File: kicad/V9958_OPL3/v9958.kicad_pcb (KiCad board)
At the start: 2 copper layers, 160 x 100.3 mm, 54 parts, among them P1 RED, P2 GREEN, P3 BLUE, P4 SYNC/C, P5 CONN_02X25, U1 74HCT139, U2 V9958, U3 DRAM_64KX4, U4 DRAM_64KX4, U5 DRAM_64KX4, U6 DRAM_64KX4, U7 cxa2075M, X1 OSC, X2 S-VIDEO, Y1 21,443Mhz

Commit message: update
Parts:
- removed C12, C9: 100n, Capacitors_ThroughHole:C_Disc_D3_P2.5
- removed X2: S-VIDEO, mini_din:mini_din-M_DIN4
- added C22: 220µF, Capacitors_ThroughHole:C_Radial_D6.3_L11.2_P2.5, F.Cu at (83.8, 88.9)
- added C23: 220µF, Capacitors_ThroughHole:C_Radial_D6.3_L11.2_P2.5, F.Cu at (83.8, 101.6)
- added U8: YMF262, Housings_SOIC:SOIC-24_7.5x15.4mm_Pitch1.27mm, F.Cu at (195.6, 71.1)
- added U9: YAC512, Housings_SOIC:SOIC-16_3.9x9.9mm_Pitch1.27mm, F.Cu at (150.2, 133.0)
- added X3: S-VIDEO, mini_din:mini_din-M_DIN4, F.Cu at (66.0, 124.5)
- C11: value 47µF -> 100n; footprint Capacitors_ThroughHole:C_Radial_D5_L11_P2.5 -> Capacitors_ThroughHole:C_Disc_D3_P2.5
- C13, C19: value 100n -> 47µF
- C14, C15, C21: value 220µF -> 100n; footprint Capacitors_ThroughHole:C_Radial_D6.3_L11.2_P2.5 -> Capacitors_ThroughHole:C_Disc_D3_P2.5
- C17: value 47µF -> 220µF; footprint Capacitors_ThroughHole:C_Radial_D5_L11_P2.5 -> Capacitors_ThroughHole:C_Radial_D6.3_L11.2_P2.5
- moved C15 110.8 mm to (194.3, 54.6), turned to 0 degrees
- moved C14 87.7 mm to (171.4, 116.8)
- moved C21 65.9 mm to (143.5, 129.5), turned to 270 degrees
- moved C11 53.8 mm to (171.4, 119.4), turned to 180 degrees
- moved C18 52.1 mm to (83.8, 128.3)
- moved C17 27.9 mm to (83.8, 63.5)
- moved C10 16.5 mm to (177.8, 129.5)
- moved C20 12.7 mm to (83.8, 76.2)
- moved C16 7.62 mm to (83.8, 120.7)
- moved R11 2.54 mm to (91.4, 99.1)
- moved R12 2.54 mm to (91.4, 96.5)
- moved C19 2.54 mm to (106.7, 82.5)
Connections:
- net /CSYNC renamed /cxa2075m/CSYNC
- C10 pad 1: /RGB_G -> VCC
- C10 pad 2: Net-(C10-Pad2) -> GND
- C11 pad 1: VCC -> /cxa2075m/RGB_B
- C11 pad 2: GND -> Net-(C11-Pad2)
- C14 pad 1: Net-(C14-Pad1) -> /cxa2075m/RGB_R
- C14 pad 2: /C_OUT -> Net-(C14-Pad2)
- C15 pad 1: Net-(C15-Pad1) -> VCC
- C15 pad 2: Net-(C15-Pad2) -> GND
- C16 pad 2: /Y_OUT -> /cxa2075m/C_OUT
- C17 pad 1: VCC -> Net-(C17-Pad1)
- C17 pad 2: GND -> Net-(C17-Pad2)
- C18 pad 2: Net-(C18-Pad2) -> /cxa2075m/Y_OUT
- C21 pad 1: Net-(C21-Pad1) -> VCC
- C21 pad 2: Net-(C21-Pad2) -> GND
- P1 pad 1: Net-(C15-Pad2) -> Net-(C17-Pad2)
- P2 pad 1: Net-(C18-Pad2) -> Net-(C20-Pad2)
- P3 pad 1: Net-(C20-Pad2) -> Net-(C22-Pad2)
- P4 pad 1: Net-(C21-Pad2) -> Net-(C23-Pad2)
- R1 pad 2: /RGB_G -> /cxa2075m/RGB_G
- R11 pad 2: Net-(C16-Pad1) -> Net-(C18-Pad1)
- R12 pad 2: Net-(C14-Pad1) -> Net-(C16-Pad1)
- R13 pad 1: Net-(C21-Pad1) -> Net-(C23-Pad1)
- R2 pad 2: /RGB_R -> /cxa2075m/RGB_R
- R3 pad 2: /RGB_B -> /cxa2075m/RGB_B
- R6 pad 2: Net-(C15-Pad1) -> Net-(C17-Pad1)
- R7 pad 2: Net-(C18-Pad1) -> Net-(C20-Pad1)
- R8 pad 2: Net-(C20-Pad1) -> Net-(C22-Pad1)
- R9 pad 2: Net-(C21-Pad1) -> Net-(C23-Pad1)
- U1 pad 10: (no net) -> Net-(U1-Pad10)
- U1 pad 11: (no net) -> Net-(U1-Pad11)
- U1 pad 12: (no net) -> Net-(U1-Pad12)
- U1 pad 13: (no net) -> GND
- U1 pad 14: (no net) -> /RW
- U1 pad 15: (no net) -> /CS_IO0
- U1 pad 9: (no net) -> Net-(U1-Pad9)
- U2 pad 22: /RGB_G -> /cxa2075m/RGB_G
- U2 pad 23: /RGB_R -> /cxa2075m/RGB_R
- U2 pad 24: /RGB_B -> /cxa2075m/RGB_B
- U7 pad 2: Net-(C12-Pad2) -> Net-(C14-Pad2)
- U7 pad 3: Net-(C10-Pad2) -> Net-(C12-Pad2)
- U7 pad 4: Net-(C9-Pad2) -> Net-(C11-Pad2)
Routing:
- net Net-(C11-Pad2): track 0.00 -> 146.6 mm
- net Net-(C9-Pad2): track 75.5 -> 0.00 mm
- net VCC: track 364.5 -> 292.0 mm
- net Net-(C10-Pad2): track 71.5 -> 0.00 mm
- net GND: track 576.9 -> 617.3 mm
- net Net-(C14-Pad1): track 26.1 -> 0.00 mm
- net Net-(C17-Pad1): track 0.00 -> 23.2 mm
- net Net-(C15-Pad1): track 23.2 -> 0.00 mm
- net Net-(C23-Pad1): track 0.00 -> 20.4 mm
- net Net-(C21-Pad1): track 20.4 -> 0.00 mm
- net Net-(C16-Pad1): track 39.0 -> 58.2 mm
- net /cxa2075m/RGB_B: track 0.00 -> 13.1 mm
- net /RGB_B: track 13.1 -> 0.00 mm
- net Net-(R12-Pad1): track 26.8 -> 39.4 mm
- net Net-(R11-Pad1): track 24.1 -> 11.5 mm
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
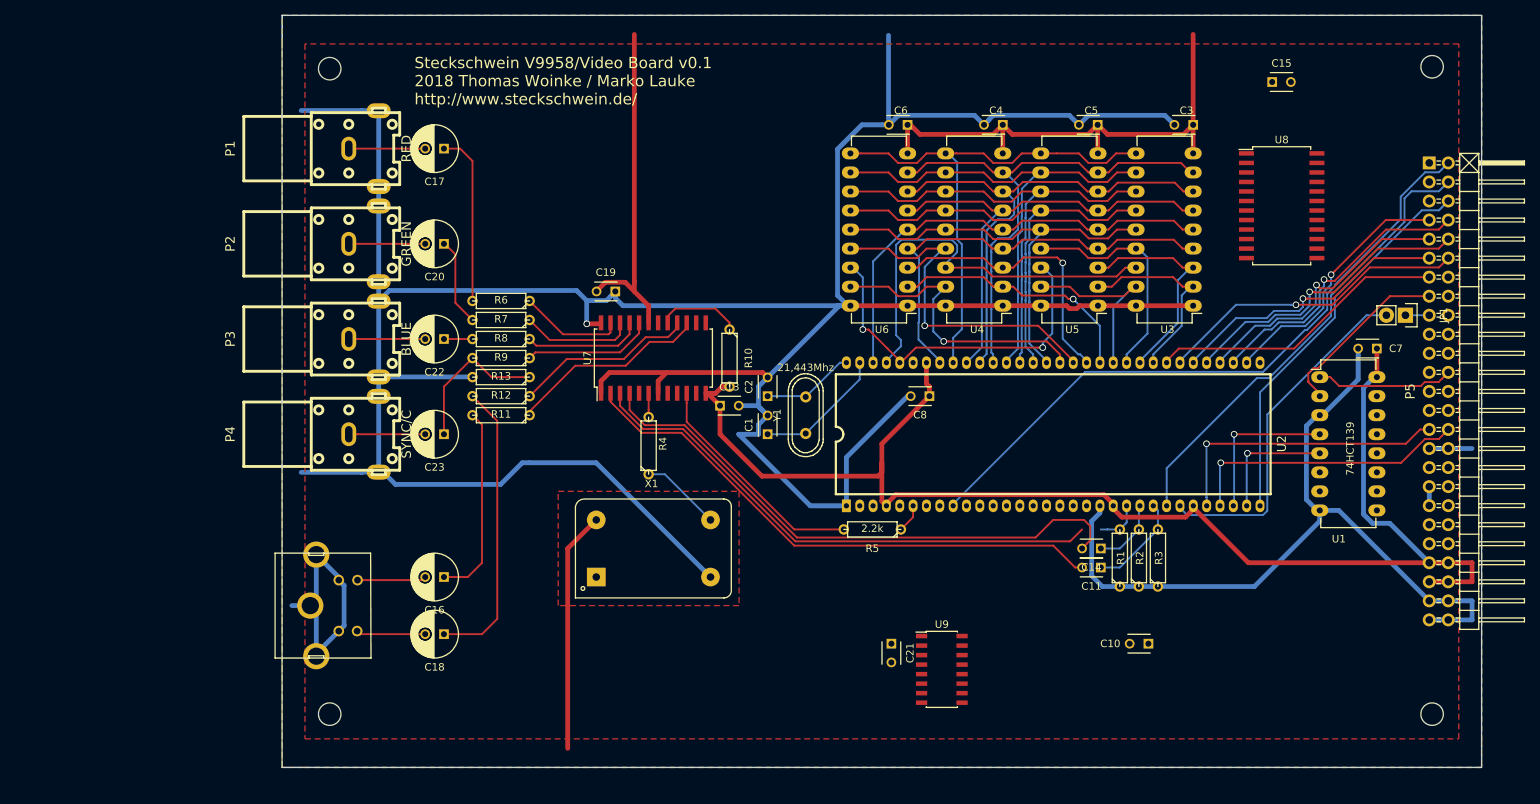
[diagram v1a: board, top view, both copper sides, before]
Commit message: dsub9-connector for RGB, pinout like 1084S D2
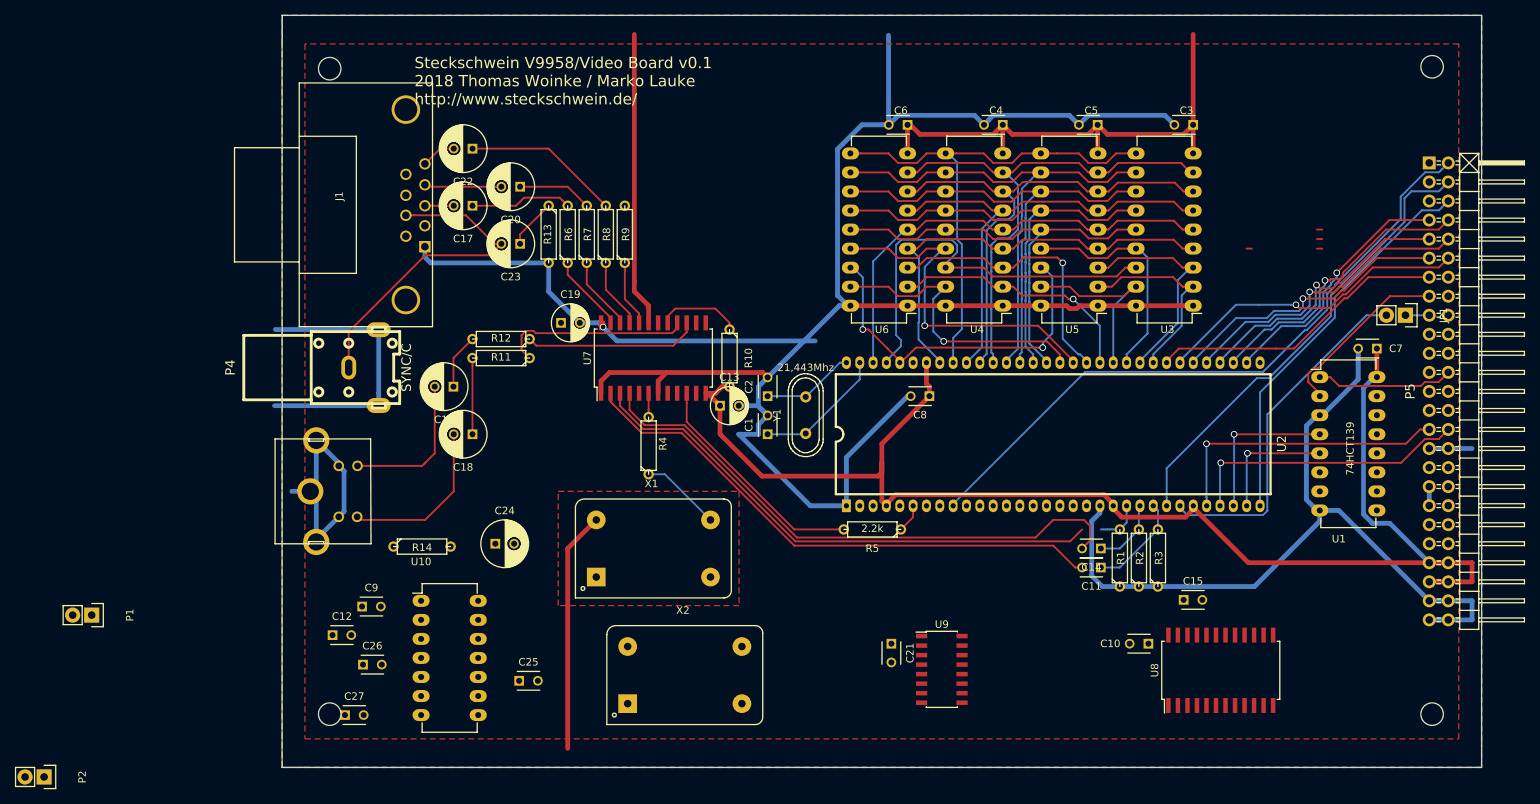
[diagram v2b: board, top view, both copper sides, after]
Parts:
- removed P3: BLUE, w_conn_av:rca_black
- added C12: 100n, Capacitors_ThroughHole:C_Disc_D3_P2.5, F.Cu at (69.0, 128.4)
- added C24: CP, Capacitors_ThroughHole:C_Radial_D6.3_L11.2_P2.5, F.Cu at (90.7, 116.2)
- added C25: C, Capacitors_ThroughHole:C_Disc_D3_P2.5, F.Cu at (93.9, 134.5)
- added C26: C, Capacitors_ThroughHole:C_Disc_D3_P2.5, F.Cu at (73.0, 132.3)
- added C27: C, Capacitors_ThroughHole:C_Disc_D3_P2.5, F.Cu at (70.6, 139.1)
- added C9: 100n, Capacitors_ThroughHole:C_Disc_D3_P2.5, F.Cu at (72.9, 124.6)
- added J1: DB9, Connect:DB9FC, F.Cu at (80.0, 71.1)
- added R14: R, Discret:R3, F.Cu at (80.9, 116.6)
- added U10: RC4136, Housings_DIP:DIP-14_W7.62mm_LongPads, F.Cu at (80.8, 123.8)
- added X2: OSC, Oscillators:KXO-200_LargePads, F.Cu at (116.0, 133.7)
- C13, C19: footprint Capacitors_ThroughHole:C_Disc_D3_P2.5 -> Capacitors_ThroughHole:C_Radial_D5_L11_P2.5
- P1: value RED -> CONN_01X02; footprint w_conn_av:rca_black -> Pin_Headers:Pin_Header_Straight_1x02
- P2: value GREEN -> CONN_01X02; footprint w_conn_av:rca_black -> Pin_Headers:Pin_Header_Straight_1x02
- moved P2 81.9 mm to (30.5, 147.3)
- moved P1 71.1 mm to (36.8, 125.7)
- moved C15 70.1 mm to (182.5, 123.7)
- moved U8 62.5 mm to (187.5, 133.1), turned to 90 degrees
- moved C23 27.4 mm to (94.0, 76.2)
- moved C18 26.9 mm to (87.6, 101.6)
- moved C22 25.7 mm to (87.6, 63.5)
- moved C16 25.4 mm to (85.1, 95.2)
- moved R9 23.3 mm to (108.0, 74.9), turned to 90 degrees
- moved R13 20.1 mm to (97.8, 74.9), turned to 270 degrees
- moved R8 19.8 mm to (105.4, 74.9), turned to 90 degrees
- moved R7 16.2 mm to (102.9, 74.9), turned to 90 degrees
- moved X3 15.2 mm to (66.0, 109.2)
- moved C20 12.7 mm to (94.0, 68.6)
- moved R6 12.6 mm to (100.3, 74.9), turned to 90 degrees
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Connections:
- P1 pad 1: Net-(C17-Pad2) -> Net-(P1-Pad1)
- P2 pad 1: Net-(C20-Pad2) -> Net-(P2-Pad1)
- U9 pad 10: Net-(U9-Pad10) -> /yac512/CH1
- U9 pad 11: Net-(U9-Pad11) -> /yac512/CH2
- U9 pad 12: Net-(U9-Pad12) -> /yac512/SWIN
- U9 pad 13: Net-(U9-Pad13) -> /yac512/AOUT
- U9 pad 14: Net-(U9-Pad14) -> /yac512/MP
- U9 pad 16: Net-(U9-Pad16) -> /yac512/CV
- U9 pad 6: Net-(U9-Pad6) -> GND
- U9 pad 9: Net-(U9-Pad9) -> GND
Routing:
- net GND: track 617.3 -> 470.9 mm
- net Net-(C16-Pad1): track 58.2 -> 7.40 mm
- net VCC: track 292.0 -> 326.4 mm
- net Net-(C23-Pad2): track 10.2 -> 44.3 mm
- net Net-(C22-Pad1): track 3.81 -> 20.9 mm
- net Net-(R12-Pad1): track 39.4 -> 23.3 mm
- net Net-(R11-Pad1): track 11.5 -> 25.6 mm
- net Net-(C23-Pad1): track 20.4 -> 6.66 mm
- net /cxa2075m/Y_OUT: track 9.25 -> 22.3 mm
- net /cxa2075m/C_OUT: track 9.20 -> 20.1 mm
- net Net-(C17-Pad1): track 23.2 -> 13.6 mm
- net Net-(R9-Pad1): track 17.4 -> 8.79 mm
- net Net-(R8-Pad1): track 15.9 -> 9.32 mm
- net Net-(C17-Pad2): track 10.2 -> 3.85 mm
- net Net-(C22-Pad2): track 10.2 -> 4.69 mm
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
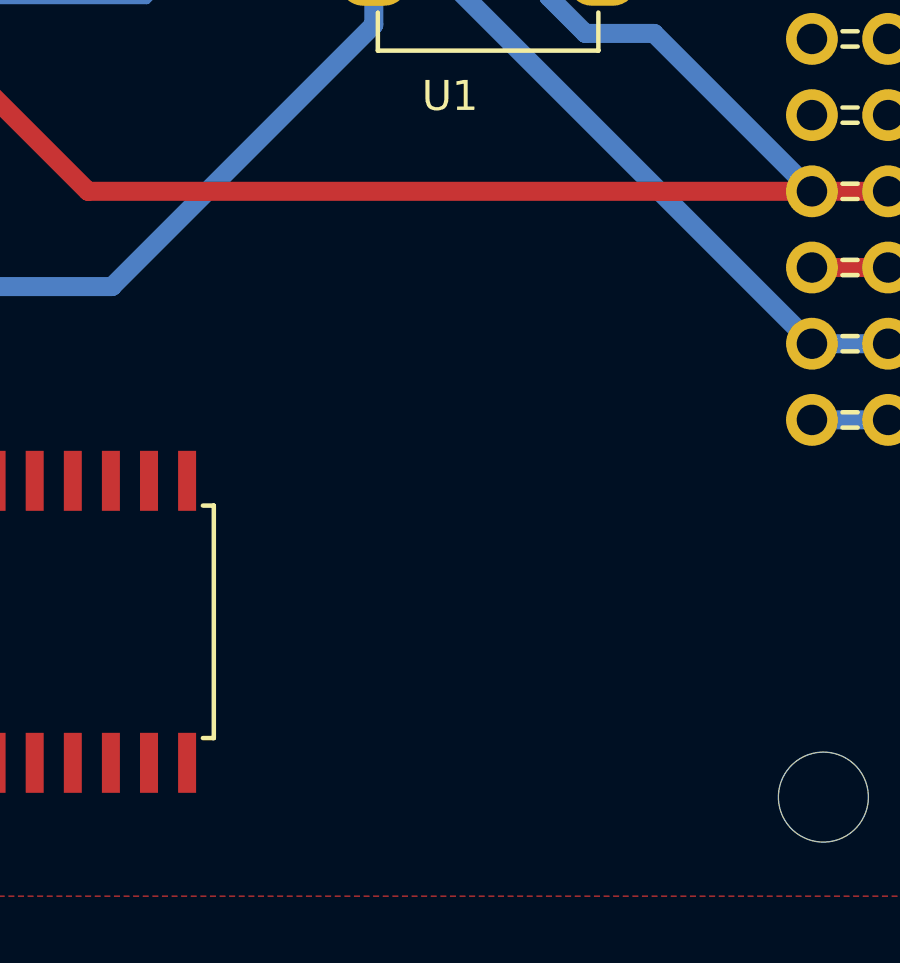
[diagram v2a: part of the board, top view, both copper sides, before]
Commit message: generate OPL2 /CSW and /CSR by using PHI2 and RDY
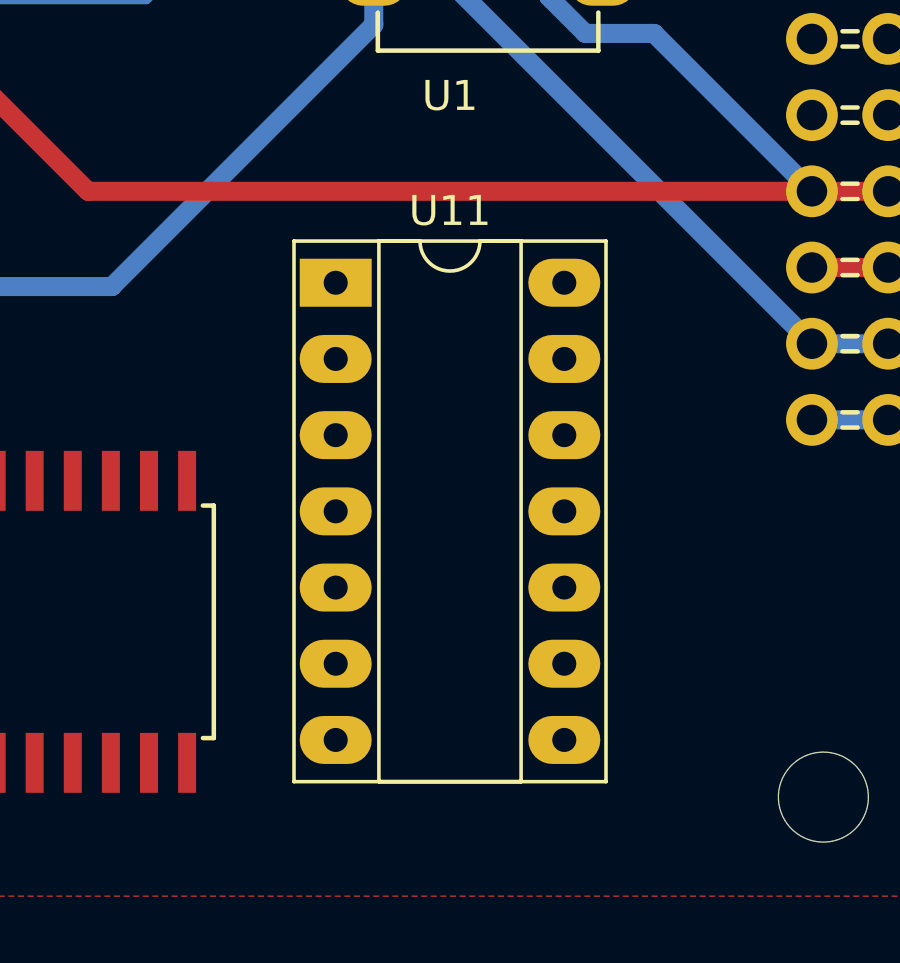
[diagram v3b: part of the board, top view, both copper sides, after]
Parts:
- added U11: 74HCT00, Housings_DIP:DIP-14_W7.62mm_Socket_LongPads, F.Cu at (199.4, 121.8)
- C24: value CP -> 10µF
- C25: value C -> 2700pF
- C26, C27: value C -> 47pF
- R14: value R -> 33
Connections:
- net /50pin connector/A0 renamed /A0
- net /50pin connector/A1 renamed /A1
- net /50pin connector/D0 renamed /D0
- net /50pin connector/D1 renamed /D1
- net /50pin connector/D2 renamed /D2
- net /50pin connector/D3 renamed /D3
- net /50pin connector/D4 renamed /D4
- net /50pin connector/D5 renamed /D5
- net /50pin connector/D6 renamed /D6
- net /50pin connector/D7 renamed /D7
- net /cxa2075m/CSYNC renamed /CSYNC
- net /cxa2075m/RGB_B renamed /RGB_B
- net /cxa2075m/RGB_G renamed /RGB_G
- net /cxa2075m/RGB_R renamed /RGB_R
- net /yac512/CLK renamed /CLK
- net /yac512/DIN renamed /DOAB
- net /yac512/SMP1 renamed /SMPBD
- net /yac512/SMP2 renamed /SMPAC
- U1 pad 1: /CS_VDP -> Net-(U1-Pad1)
- U1 pad 13: GND -> Net-(U1-Pad13)
- U1 pad 2: /RW -> Net-(U1-Pad2)
- U1 pad 3: GND -> Net-(U1-Pad3)
- U2 pad 30: Net-(U1-Pad4) -> Net-(U2-Pad30)
- U2 pad 31: Net-(U1-Pad5) -> Net-(U2-Pad31)
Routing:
- net Net-(U1-Pad1): track 0.00 -> 16.6 mm
- net /CS_VDP: track 18.4 -> 1.83 mm
- net Net-(U2-Pad30): track 0.00 -> 9.59 mm
- net Net-(U1-Pad4): track 21.0 -> 11.4 mm
- net Net-(U1-Pad3): track 0.00 -> 9.48 mm
- net GND: track 470.9 -> 461.5 mm
- net Net-(U2-Pad31): track 0.00 -> 6.91 mm
- net Net-(U1-Pad5): track 16.7 -> 9.79 mm
- net Net-(U1-Pad2): track 0.00 -> 3.00 mm
- net /RW: track 24.6 -> 21.6 mm
